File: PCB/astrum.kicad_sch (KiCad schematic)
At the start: 52 parts, among them J1 USB_C_Receptacle_USB2.0_16P, J10 Conn_01x05_Pin, J11 Screw_Terminal_01x02, J2 Micro_SD_Card, J3 Screw_Terminal_01x02, J5 Conn_01x04_MountingPin, J6 Conn_01x04_MountingPin, J7 Conn_01x10_Pin, J8 Conn_01x10_Pin, J9 Conn_01x05_Pin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

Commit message: update production files
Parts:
- added C21: 100nF, A_HDJ_Library:C_0603_1608Metric, symbol Device:C
- added C22: 100nF, A_HDJ_Library:C_0402_1005Metric, symbol Device:C
- added R6: 4.7k, Resistor_SMD:R_0603_1608Metric, symbol Device:R
- added R8: 10k, Resistor_SMD:R_0603_1608Metric, symbol Device:R
- added SW1, SW2: TS-1088-AR02016, easyeda2kicad:SW-SMD_L3.9-W3.0-P4.45, symbol ASM1166:TS-1088-AR02016
- C18: value C_Polarized_Small -> 22uF
- C2: footprint A_HDJ_Library:C_0603_1608Metric -> lpddr4-testbed-footprints:C_0402_1005Metric
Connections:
- net GND: now also C21.2, C22.2, R8.1, SW1.2
- net VDD: now also C22.1, R6.2, SW2.2
- net at J2.2 (DAT3/CD), U1.25 (PB12): now also R6.1
- net BOOT0: now reaches U1.44 (BOOT0)
- net BOOT0: now also R8.2, SW2.1
- net NRST: now reaches U1.7 (NRST)
- net NRST: now also C21.1, SW1.1
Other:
- moved on the sheet: C1, C10, C11, C12, C13, C14, C15, C16, C17, C18, C19, C2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

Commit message: make the board cheaper?
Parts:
- removed C14: 100nF, A_HDJ_Library:C_0603_1608Metric, symbol Device:C
- removed U5: ICM-20948, Sensor_Motion:InvenSense_QFN-24_3x3mm_P0.4mm, symbol Sensor_Motion:ICM-20948
- removed U6: MIC5317-1.8xM5, Package_TO_SOT_SMD:SOT-23-5, symbol Regulator_Linear:MIC5317-1.8xM5
- removed Y1: 25 mHz, Crystal:Crystal_SMD_Abracon_ABM3-2Pin_5.0x3.2mm, symbol Device:Crystal
- added R10, R9: 10k, Resistor_SMD:R_0603_1608Metric, symbol Device:R
- added U11: LD39015M18R, Package_TO_SOT_SMD:SOT-23-5, symbol Regulator_Linear:LD39015M18R
- added U6: LSM6DSR, LGA_M6DSR_STM, symbol 2025-12-13_23-42-40:LSM6DSR
- added Y2: 25mHz, Crystal:Crystal_SMD_3225-4Pin_3.2x2.5mm, symbol Device:Crystal_GND24
- C12, C13, R5, R7, U10, U7: now not fitted; now left out of the parts list
- C18: footprint Capacitor_SMD:CP_Elec_3x5.3 -> Capacitor_SMD:CP_Elec_4x5.4
- C20: value C_Polarized_Small -> 22uF; footprint Capacitor_SMD:CP_Elec_3x5.3 -> Capacitor_SMD:CP_Elec_4x5.4
- C7, C8: value 5.6pF -> 12pF
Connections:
- net +1V8: now also U11.5 (OUT); no longer C15.1, C16.1
- net GND: now also J7.10 (Pin_10), J7.9 (Pin_9), U11.2 (GND), U6.6 (GND), U6.7 (GND), Y2.2, Y2.4
- net GPIO8: now also U6.4 (INT1); no longer J8.10 (Pin_10)
- net IMU_INT: now also U6.9 (INT2)
- net IMU_SCL: now also R10.2, U6.13 (SCL)
- net IMU_SDA: now also R9.2, U6.14 (SDA)
- net VDD: now also C15.1, C16.1, R10.1, R9.1, U11.1 (IN), U11.3 (EN), U6.12 (CS), U6.5 (VDDIO), U6.8 (VDD)
- net at C7.2, U1.5 (PH0): now also Y2.3
- net at C8.2, U1.6 (PH1): now also Y2.1
- no-connect marks 4 -> 7
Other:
- moved on the sheet: C1, C10, C11, C15, C16, C17, C19, C2, C21, C22, C3, C4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

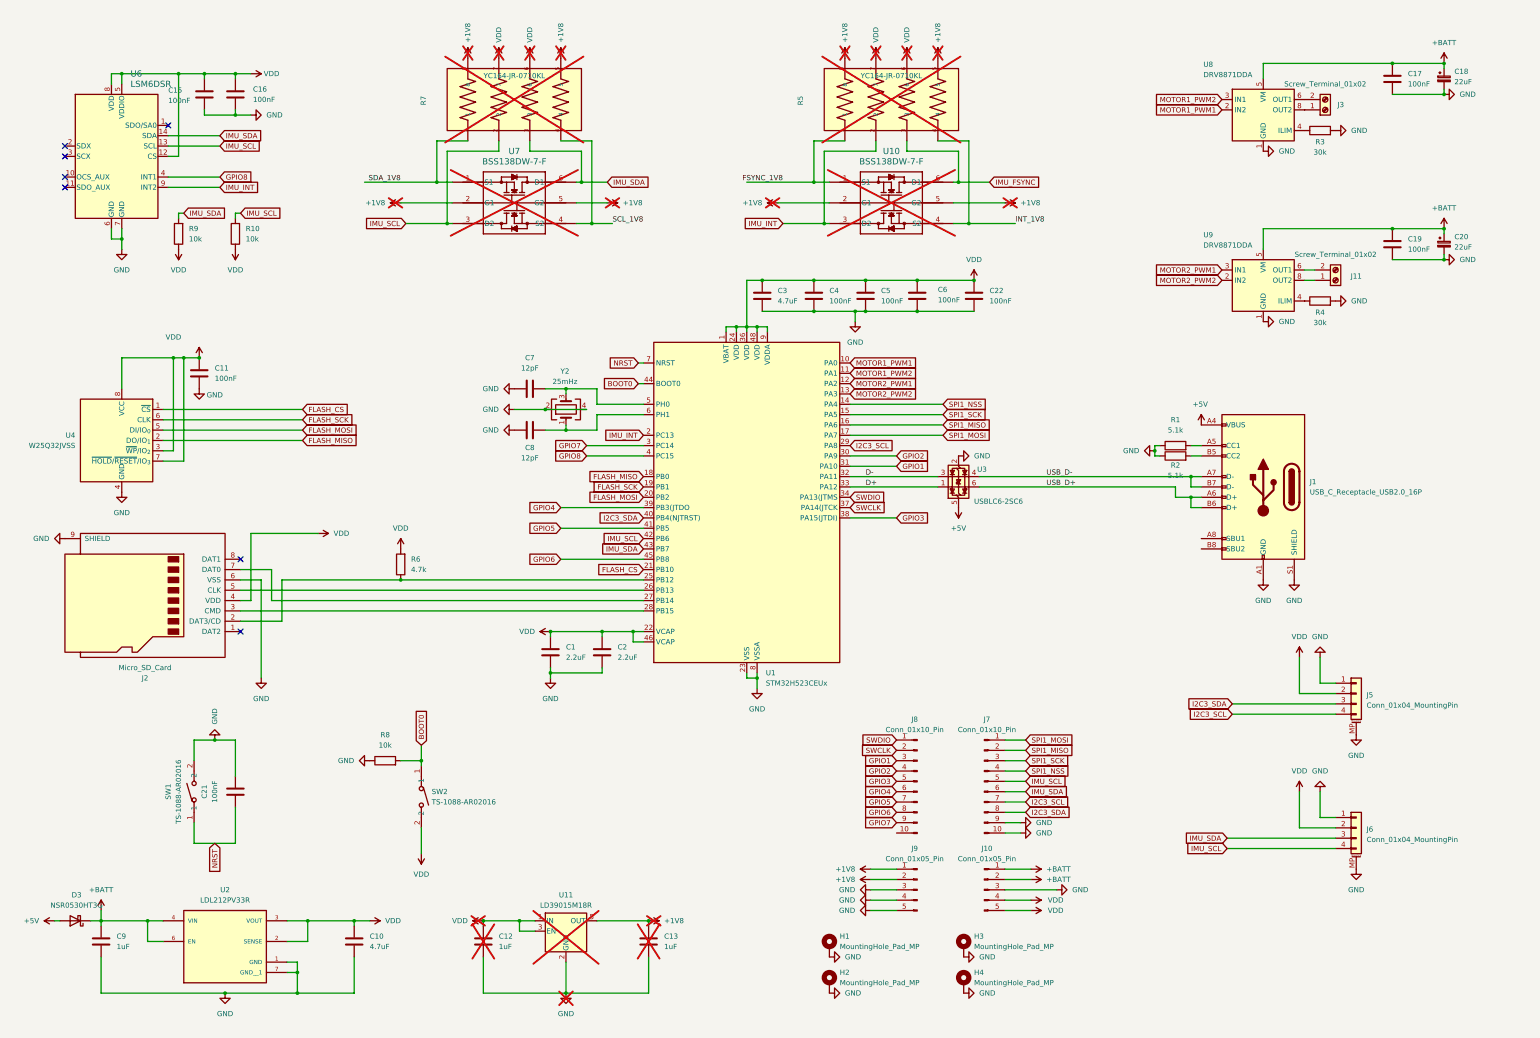
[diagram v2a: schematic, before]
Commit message: fix oscillator
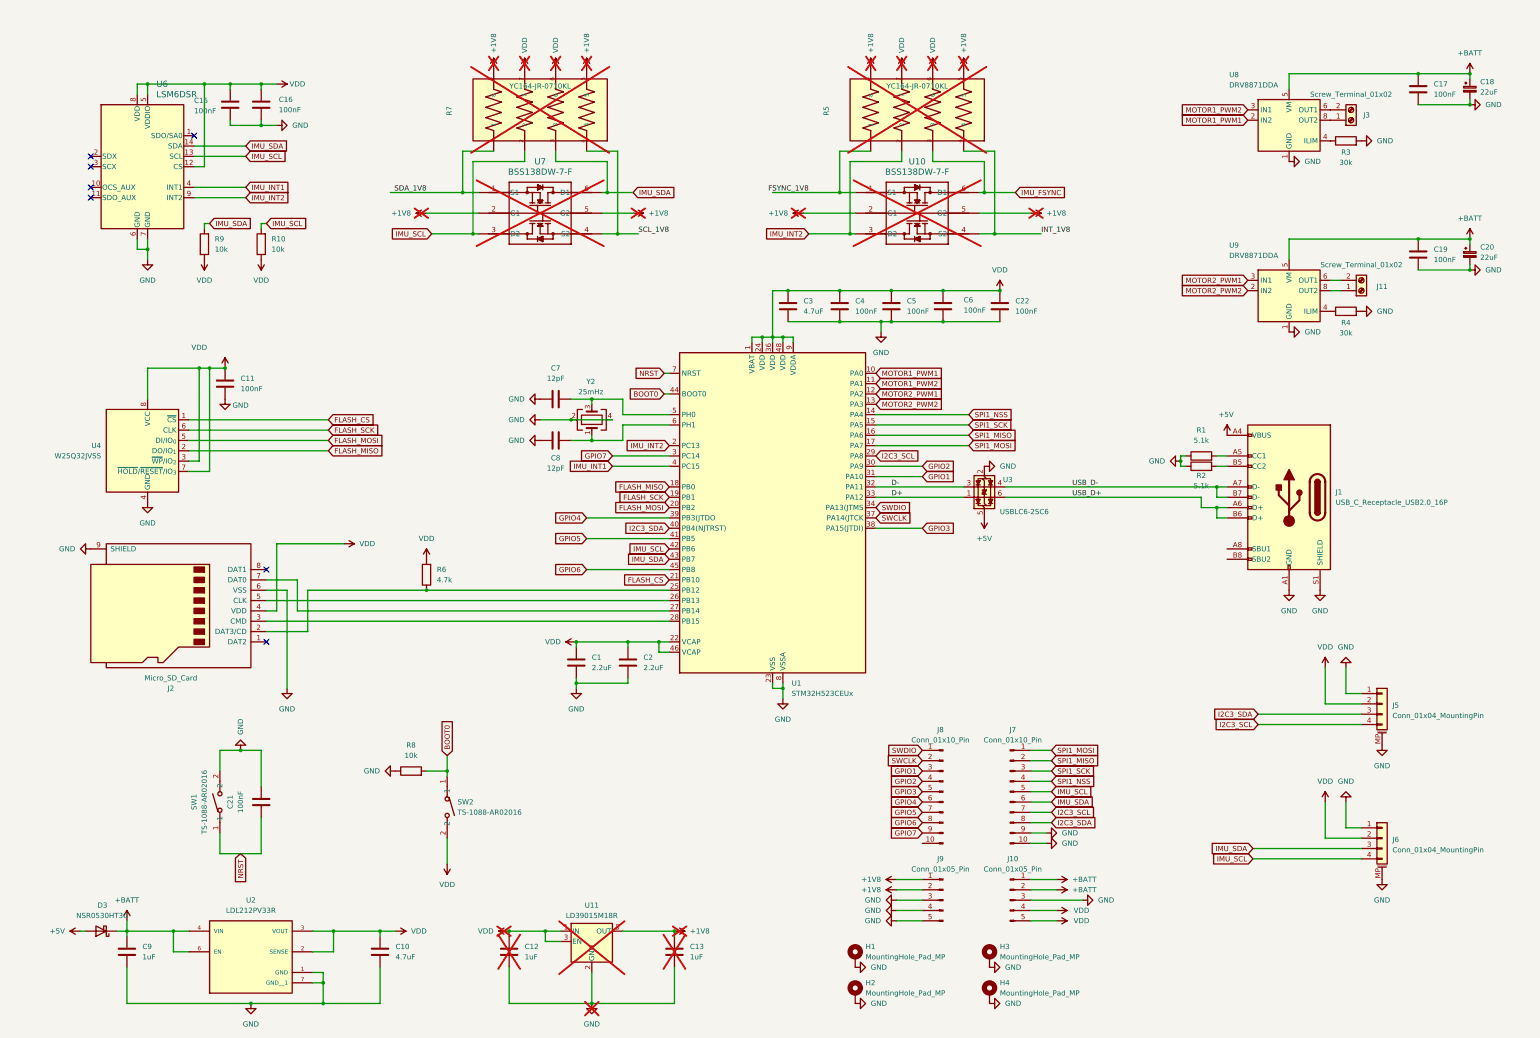
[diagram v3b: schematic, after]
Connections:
- net GPIO8 renamed IMU_INT1
- net IMU_INT renamed IMU_INT2
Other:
- company: (none) -> Nanuet Science Olympiads
- title: Astrum Robot Controller -> AERO ROBOT CONTROLLER
- moved on the sheet: C1, C10, C11, C12, C13, C15, C16, C17, C18, C19, C2, C20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
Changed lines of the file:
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@@
 	(paper "A3")
 	(title_block
-		(title "Astrum Robot Controller")
-		(rev "Rev 1.0")
+		(title "AERO ROBOT CONTROLLER")
+		(rev "1.0")
+		(company "Nanuet Science Olympiads")
+		(comment 1 "Brian Guan")
 	)

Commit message: fix some dum vcap thingies
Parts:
- U2: footprint LDL212PV33R:SON50P200X200X80-7N -> LDL212PV33R:DFN_V33R_STM
- U6: footprint LGA_M6DSR_STM -> LSM6DSR:LGA_M6DSR_STM
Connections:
- net IMU_INT2: no longer U1.2 (PC13), U6.9 (INT2)
- net VDD: no longer C1.1, C2.1, U1.22 (VCAP), U1.46 (VCAP)
- new net: C1.1, C2.1, U1.22 (VCAP), U1.46 (VCAP)
- new net IMU_INT: U1.2 (PC13), U6.9 (INT2)

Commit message: update stuff again
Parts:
- C7, C8: value 12pF -> 18pF
- U6: footprint LSM6DSR:LGA_M6DSR_STM -> LGA_M6DSR_STM
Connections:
- net IMU_INT2 is gone; now on net IMU_INT: R5.2, U10.3 (D2)
- net IMU_INT1 renamed GPIO8
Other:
- moved on the sheet: C1, C10, C11, C12, C13, C15, C16, C17, C18, C19, C2, C20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
